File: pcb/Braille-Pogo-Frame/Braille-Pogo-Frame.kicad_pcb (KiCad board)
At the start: 2 copper layers, 74 x 40 mm, 24 parts, among them J101 Conn_01x06, J102 Conn_01x06, J103 Conn_01x06, J104 Conn_01x06, J105 Conn_01x06, J106 Conn_01x06, J107 Conn_01x06, J108 Conn_01x06

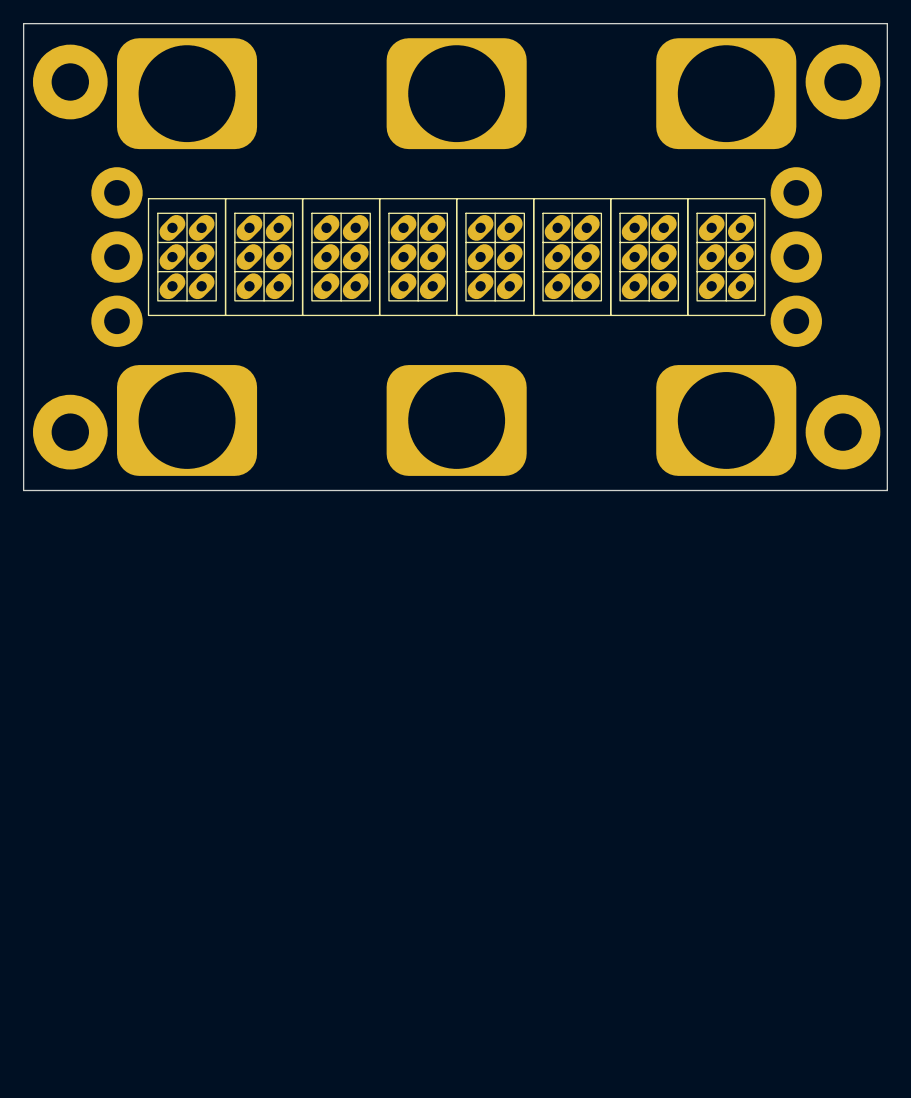
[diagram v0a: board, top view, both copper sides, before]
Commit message: Move PCB down
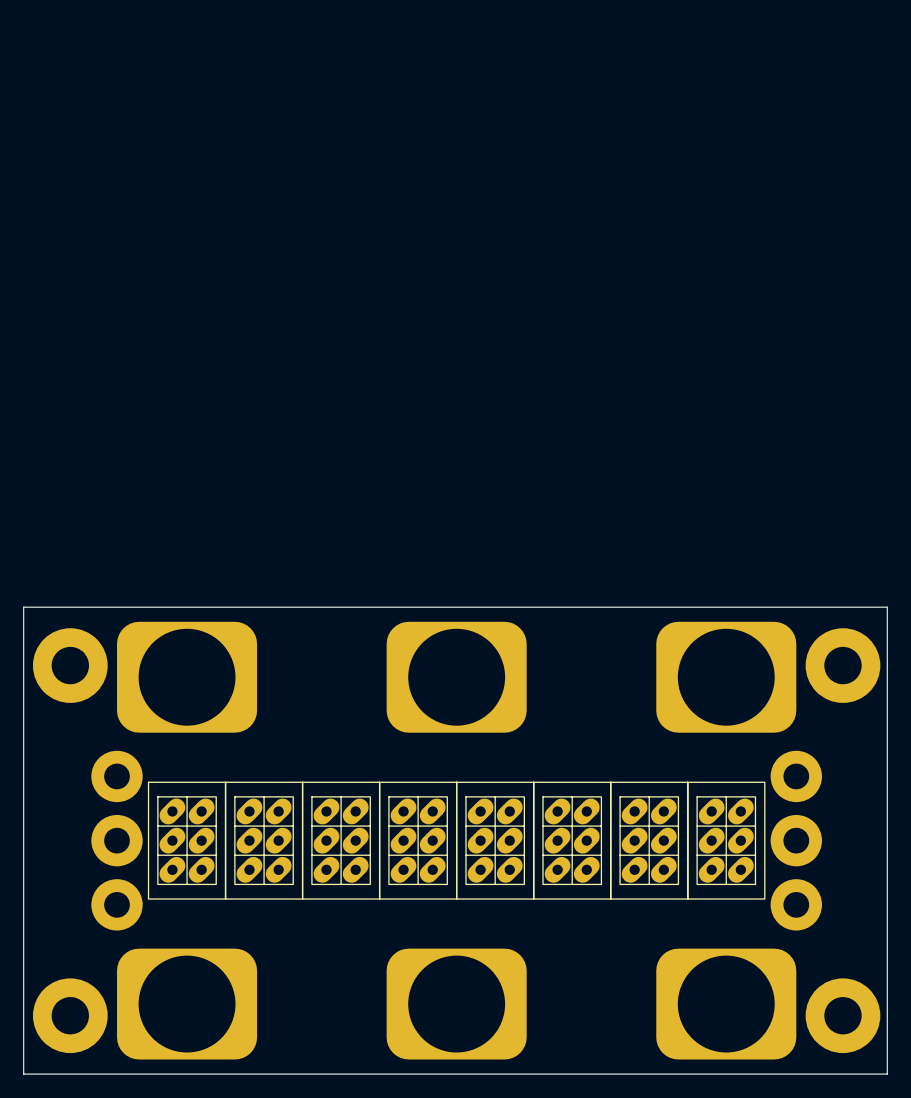
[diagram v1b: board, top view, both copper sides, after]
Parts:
- moved H101 50.0 mm to (123.1, 86.0)
- moved H102 50.0 mm to (123.1, 114.0)
- moved H103 50.0 mm to (146.2, 86.0)
- moved H104 50.0 mm to (100.0, 114.0)
- moved H105 50.0 mm to (100.0, 86.0)
- moved H106 50.0 mm to (146.2, 114.0)
- moved H107 50.0 mm to (94.0, 94.5)
- moved H108 50.0 mm to (94.0, 105.5)
- moved H109 50.0 mm to (152.2, 94.5)
- moved H110 50.0 mm to (152.2, 105.5)
- moved H111 50.0 mm to (94.0, 100.0)
- moved H112 50.0 mm to (152.2, 100.0)
- moved H113 50.0 mm to (90.0, 85.0)
- moved H114 50.0 mm to (156.2, 85.0)
- moved H115 50.0 mm to (156.2, 115.0)
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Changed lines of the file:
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@@
 	(footprint "00-lib-footprints:Braille_Cell_Pogos_Solder_2.5mmIntra_6.6x10mmInter"
 		(layer "F.Cu")
-		(at 100 50)
+		(at 100 100)
 		(property "Reference" "J101"
 			(at 0 5.1 0)
@@
 	(footprint "00-lib-footprints:Braille_Cell_Pogos_Solder_2.5mmIntra_6.6x10mmInter"
 		(layer "F.Cu")
-		(at 133 50)
+		(at 133 100)
 		(property "Reference" "J106"
 			(at 0 5.1 0)
@@
 	(footprint "00-lib-footprints:MountingHole_2.2mm_M2_Pad_NoSilk"
 		(layer "F.Cu")
-		(at 152.2 50)
+		(at 152.2 100)
 		(descr "Mounting Hole 2.2mm, M2")
 		(tags "mounting hole 2.2mm m2")
@@
 	(footprint "00-lib-footprints:MountingHole_8mm_Rect_NoSilk"
 		(layer "F.Cu")
-		(at 100 64)
+		(at 100 114)
 		(descr "Mounting Hole 8.4mm, M8")
 		(tags "mounting hole 8.4mm m8")
@@
 	(footprint "00-lib-footprints:MountingHole_2.2mm_M2_Pad_NoSilk"
 		(layer "F.Cu")
-		(at 152.2 55.5)
+		(at 152.2 105.5)
 		(descr "Mounting Hole 2.2mm, M2")
 		(tags "mounting hole 2.2mm m2")
@@
 	(footprint "00-lib-footprints:MountingHole_8mm_Rect_NoSilk"
 		(layer "F.Cu")
-		(at 146.2 64)
+		(at 146.2 114)
 		(descr "Mounting Hole 8.4mm, M8")
 		(tags "mounting hole 8.4mm m8")
@@
 	(footprint "00-lib-footprints:Braille_Cell_Pogos_Solder_2.5mmIntra_6.6x10mmInter"
 		(layer "F.Cu")
-		(at 139.6 50)
+		(at 139.6 100)
 		(property "Reference" "J107"
 			(at 0 5.1 0)
@@
 	(footprint "00-lib-footprints:MountingHole_2.2mm_M2_Pad_NoSilk"
 		(layer "F.Cu")
-		(at 94 44.5)
+		(at 94 94.5)
 		(descr "Mounting Hole 2.2mm, M2")
 		(tags "mounting hole 2.2mm m2")
@@
 	(footprint "00-lib-footprints:MountingHole_8mm_Rect_NoSilk"
 		(layer "F.Cu")
-		(at 146.2 36)
+		(at 146.2 86)
 		(descr "Mounting Hole 8.4mm, M8")
 		(tags "mounting hole 8.4mm m8")
@@
 	(footprint "00-lib-footprints:MountingHole_2.2mm_M2_Pad_NoSilk"
 		(layer "F.Cu")
-		(at 94 55.5)
+		(at 94 105.5)
 		(descr "Mounting Hole 2.2mm, M2")
 		(tags "mounting hole 2.2mm m2")
@@
 	(footprint "00-lib-footprints:Braille_Cell_Pogos_Solder_2.5mmIntra_6.6x10mmInter"
 		(layer "F.Cu")
-		(at 106.6 50)
+		(at 106.6 100)
 		(property "Reference" "J103"
 			(at 0 5.1 0)
@@
 	(footprint "00-lib-footprints:MountingHole_8mm_Rect_NoSilk"
 		(layer "F.Cu")
-		(at 123.1 36)
+		(at 123.1 86)
 		(descr "Mounting Hole 8.4mm, M8")
 		(tags "mounting hole 8.4mm m8")
@@
 	(footprint "00-lib-footprints:Braille_Cell_Pogos_Solder_2.5mmIntra_6.6x10mmInter"
 		(layer "F.Cu")
-		(at 146.2 50)
+		(at 146.2 100)
 		(property "Reference" "J108"
 			(at 0 5.1 0)
@@
 	(footprint "00-lib-footprints:MountingHole_2.2mm_M2_Pad_NoSilk"
 		(layer "F.Cu")
-		(at 94 50)
+		(at 94 100)
 		(descr "Mounting Hole 2.2mm, M2")
 		(tags "mounting hole 2.2mm m2")
@@
 	(footprint "00-lib-footprints:Braille_Cell_Pogos_Solder_2.5mmIntra_6.6x10mmInter"
 		(layer "F.Cu")
-		(at 113.2 50)
+		(at 113.2 100)
 		(property "Reference" "J102"
 			(at 0 5.1 0)
@@
 	(footprint "00-lib-footprints:MountingHole_2.2mm_M2_Pad_NoSilk"
 		(layer "F.Cu")
-		(at 152.2 44.5)
+		(at 152.2 94.5)
 		(descr "Mounting Hole 2.2mm, M2")
 		(tags "mounting hole 2.2mm m2")
@@
 	(footprint "00-lib-footprints:MountingHole_3.2mm_M3_Pad_NoSilk"
 		(layer "F.Cu")
-		(at 156.2 65)
+		(at 156.2 115)
 		(descr "Mounting Hole 3.2mm, M3")
 		(tags "mounting hole 3.2mm m3")
@@
 	(footprint "00-lib-footprints:MountingHole_8mm_Rect_NoSilk"
 		(layer "F.Cu")
-		(at 123.1 64)
+		(at 123.1 114)
 		(descr "Mounting Hole 8.4mm, M8")
 		(tags "mounting hole 8.4mm m8")
@@
 	(footprint "00-lib-footprints:MountingHole_3.2mm_M3_Pad_NoSilk"
 		(layer "F.Cu")
-		(at 90 35)
+		(at 90 85)
 		(descr "Mounting Hole 3.2mm, M3")
 		(tags "mounting hole 3.2mm m3")
@@
 	(footprint "00-lib-footprints:MountingHole_3.2mm_M3_Pad_NoSilk"
 		(layer "F.Cu")
-		(at 156.2 35)
+		(at 156.2 85)
 		(descr "Mounting Hole 3.2mm, M3")
 		(tags "mounting hole 3.2mm m3")
@@
 	(footprint "00-lib-footprints:MountingHole_3.2mm_M3_Pad_NoSilk"
 		(layer "F.Cu")
-		(at 90 65)
+		(at 90 115)
 		(descr "Mounting Hole 3.2mm, M3")
 		(tags "mounting hole 3.2mm m3")
@@
 	(footprint "00-lib-footprints:MountingHole_8mm_Rect_NoSilk"
 		(layer "F.Cu")
-		(at 100 36)
+		(at 100 86)
 		(descr "Mounting Hole 8.4mm, M8")
 		(tags "mounting hole 8.4mm m8")
@@
 	(footprint "00-lib-footprints:Braille_Cell_Pogos_Solder_2.5mmIntra_6.6x10mmInter"
 		(layer "F.Cu")
-		(at 119.8 50)
+		(at 119.8 100)
 		(property "Reference" "J104"
 			(at 0 5.1 0)
@@
 	(footprint "00-lib-footprints:Braille_Cell_Pogos_Solder_2.5mmIntra_6.6x10mmInter"
 		(layer "F.Cu")
-		(at 126.4 50)
+		(at 126.4 100)
 		(property "Reference" "J105"
 			(at 0 5.1 0)
@@
 	)
 	(gr_rect
-		(start 121.75 41)
-		(end 148 44.5)
+		(start 121.75 91)
+		(end 148 94.5)
 		(stroke
 			(width 0.1)
@@
 	)
 	(gr_rect
-		(start 105.5 40)
-		(end 117 44.5)
+		(start 105.5 90)
+		(end 117 94.5)
 		(stroke
 			(width 0.1)
@@
 	)
 	(gr_rect
-		(start 86 30)
-		(end 160 70)
+		(start 86 80)
+		(end 160 120)
 		(stroke
 			(width 0.05)
@@
 	)
 	(gr_text "Braille Display (Pogo + Solenoid)\n2024-10-10"
-		(at 148 44.25 0)
+		(at 148 94.25 0)
 		(layer "B.SilkS")
 		(effects
@@
 	)
 	(gr_text "6.6mm Inter-Cell\n2.5mm Intra-Cell\nM2, M3, and 8mm"
-		(at 116.75 44 0)
+		(at 116.75 94 0)
 		(layer "B.SilkS")
 		(effects

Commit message: Refactor Braille Cells, add Stepper footprint
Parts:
- renumbered H101 to H1, H110 to H10, H111 to H11, H112 to H12, H113 to H13, H114 to H14, H115 to H15, H116 to H16, H102 to H2, H103 to H3, H104 to H4, H105 to H5, H106 to H6, H107 to H7, H108 to H8, H109 to H9, J101 to J1, J102 to J2, J103 to J3, J104 to J4, J105 to J5, J106 to J6, J107 to J7, J108 to J8

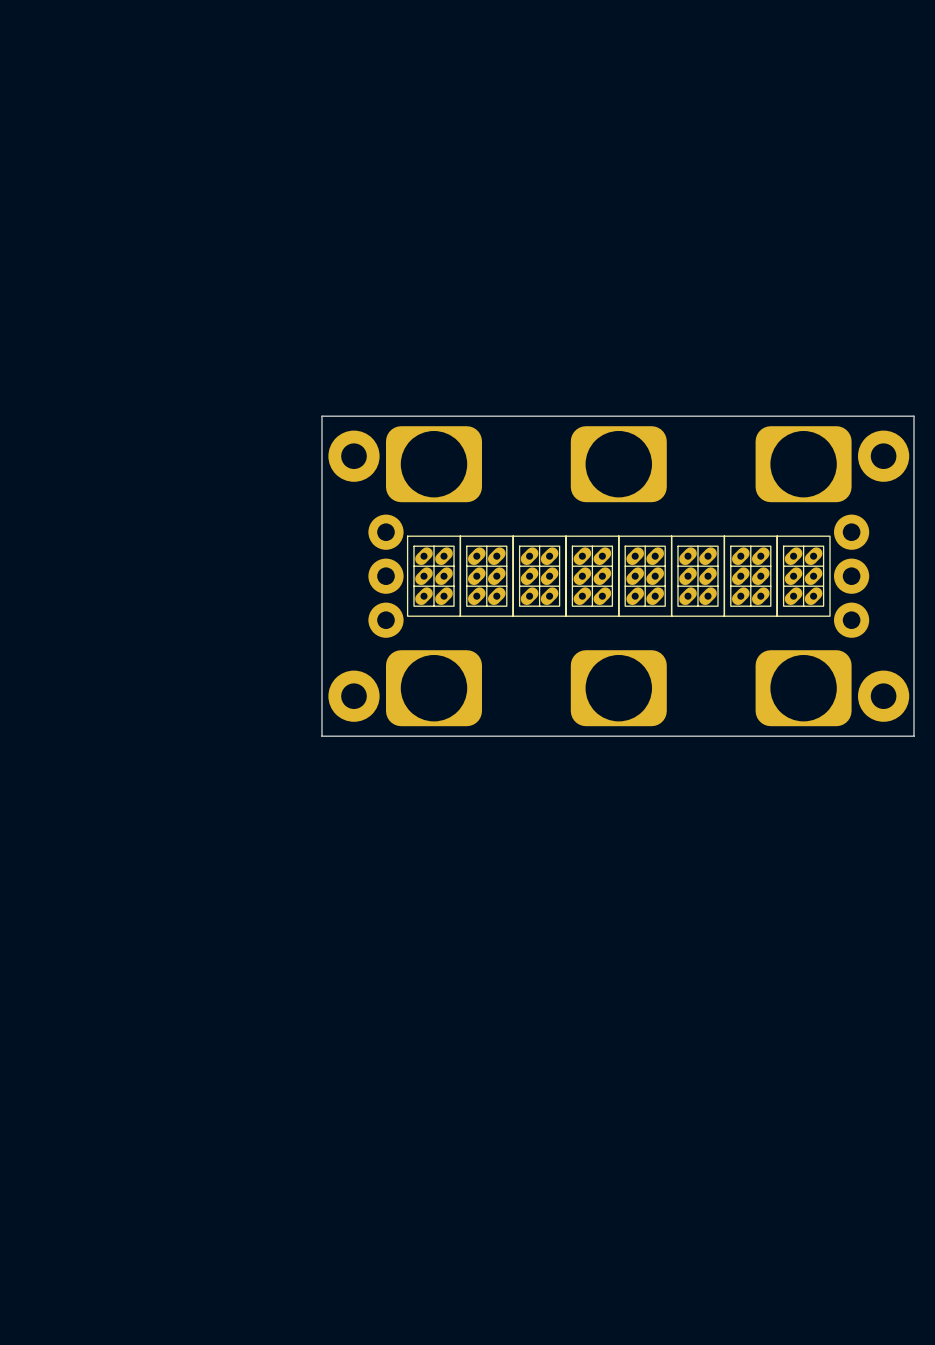
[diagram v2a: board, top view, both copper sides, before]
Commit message: PCB: Place motor drivers and horiz. rail mounts
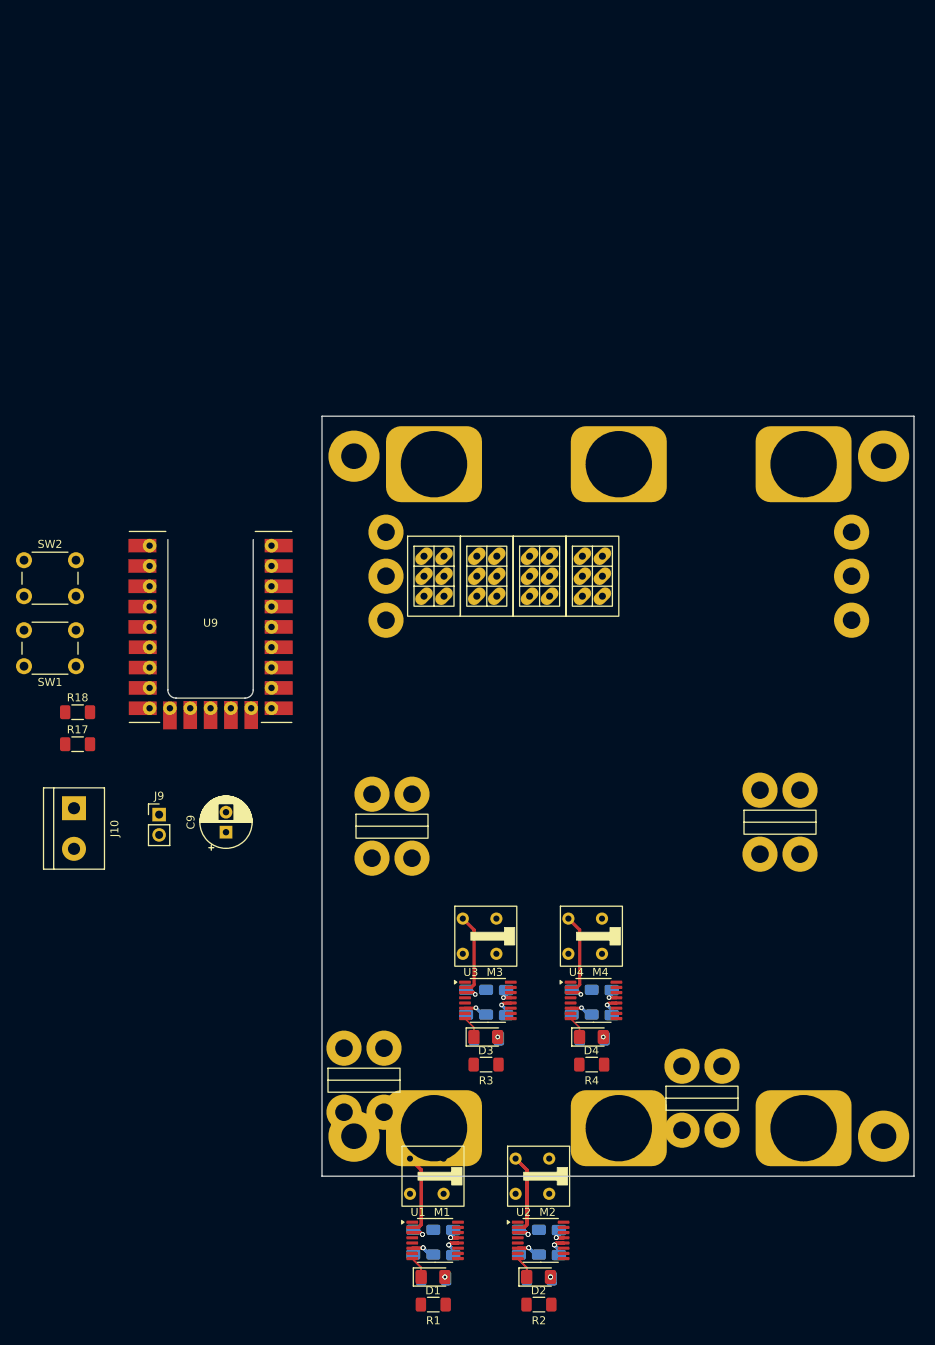
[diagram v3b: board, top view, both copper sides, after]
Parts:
- removed J5, J6, J7, J8: Conn_01x06, 00-lib-footprints:Braille_Cell_Pogos_Solder_2.5mmIntra_6.6x10mmInter
- added C1: 100n, Capacitor_SMD:C_1206_3216Metric_Pad1.33x1.80mm_HandSolder, B.Cu at (102.4, 183.3)
- added C2: 100n, Capacitor_SMD:C_1206_3216Metric_Pad1.33x1.80mm_HandSolder, B.Cu at (115.6, 183.3)
- added C3: 100n, Capacitor_SMD:C_1206_3216Metric_Pad1.33x1.80mm_HandSolder, B.Cu at (109.0, 153.3)
- added C4: 100n, Capacitor_SMD:C_1206_3216Metric_Pad1.33x1.80mm_HandSolder, B.Cu at (122.2, 153.3)
- added C9: 10u, Capacitor_THT:CP_Radial_D6.3mm_P2.50mm, F.Cu at (74.0, 132.0)
- added D1: LED, LED_SMD:LED_1206_3216Metric_Pad1.42x1.75mm_HandSolder, F.Cu at (99.9, 187.6)
- added D2: LED, LED_SMD:LED_1206_3216Metric_Pad1.42x1.75mm_HandSolder, F.Cu at (113.1, 187.6)
- added D3: LED, LED_SMD:LED_1206_3216Metric_Pad1.42x1.75mm_HandSolder, F.Cu at (106.5, 157.6)
- added D4: LED, LED_SMD:LED_1206_3216Metric_Pad1.42x1.75mm_HandSolder, F.Cu at (119.7, 157.6)
- added H17: MountingHole_Pad, 00-lib-footprints:HorizMounting_4x_M2_and_M3_Middle, F.Cu at (94.8, 131.2)
- added H18: MountingHole_Pad, 00-lib-footprints:HorizMounting_4x_M2_and_M3_Middle, F.Cu at (91.2, 163.0)
- added H19: MountingHole_Pad, 00-lib-footprints:HorizMounting_4x_M2_and_M3_Middle, F.Cu at (143.2, 130.8)
- added H20: MountingHole_Pad, 00-lib-footprints:HorizMounting_4x_M2_and_M3_Middle, F.Cu at (133.5, 165.2)
- added J10: Screw_Terminal_01x02, TerminalBlock:TerminalBlock_bornier-2_P5.08mm, F.Cu at (55.0, 129.0)
- added J9: Conn_01x02, Connector_PinHeader_2.54mm:PinHeader_1x02_P2.54mm_Vertical, F.Cu at (65.6, 129.8)
- added M1: Stepper_Motor_bipolar, 00-lib-footprints:MicroStepper_8mm-2mmGear, F.Cu at (100.0, 175.0)
- added M2: Stepper_Motor_bipolar, 00-lib-footprints:MicroStepper_8mm-2mmGear, F.Cu at (113.2, 175.0)
- added M3: Stepper_Motor_bipolar, 00-lib-footprints:MicroStepper_8mm-2mmGear, F.Cu at (106.6, 145.0)
- added M4: Stepper_Motor_bipolar, 00-lib-footprints:MicroStepper_8mm-2mmGear, F.Cu at (119.8, 145.0)
- added R1: 5k1, Resistor_SMD:R_1206_3216Metric_Pad1.30x1.75mm_HandSolder, F.Cu at (99.9, 191.1)
- added R10: 2k1, Resistor_SMD:R_1206_3216Metric_Pad1.30x1.75mm_HandSolder, B.Cu at (113.2, 187.8)
- added R11: 2k1, Resistor_SMD:R_1206_3216Metric_Pad1.30x1.75mm_HandSolder, B.Cu at (106.6, 157.8)
- added R12: 2k1, Resistor_SMD:R_1206_3216Metric_Pad1.30x1.75mm_HandSolder, B.Cu at (119.8, 157.8)
- added R17: 5k1, Resistor_SMD:R_1206_3216Metric_Pad1.30x1.75mm_HandSolder, F.Cu at (55.5, 121.0)
- added R18: 5k1, Resistor_SMD:R_1206_3216Metric_Pad1.30x1.75mm_HandSolder, F.Cu at (55.5, 117.0)
- added R19: 330m, Resistor_SMD:R_1206_3216Metric_Pad1.30x1.75mm_HandSolder, B.Cu at (99.9, 183.2)
- added R2: 5k1, Resistor_SMD:R_1206_3216Metric_Pad1.30x1.75mm_HandSolder, F.Cu at (113.1, 191.1)
- added R20: 330m, Resistor_SMD:R_1206_3216Metric_Pad1.30x1.75mm_HandSolder, B.Cu at (113.1, 183.2)
- added R21: 330m, Resistor_SMD:R_1206_3216Metric_Pad1.30x1.75mm_HandSolder, B.Cu at (106.5, 153.2)
- added R22: 330m, Resistor_SMD:R_1206_3216Metric_Pad1.30x1.75mm_HandSolder, B.Cu at (119.7, 153.2)
- added R27: 330m, Resistor_SMD:R_1206_3216Metric_Pad1.30x1.75mm_HandSolder, B.Cu at (97.4, 183.2)
- added R28: 330m, Resistor_SMD:R_1206_3216Metric_Pad1.30x1.75mm_HandSolder, B.Cu at (110.6, 183.2)
- added R29: 330m, Resistor_SMD:R_1206_3216Metric_Pad1.30x1.75mm_HandSolder, B.Cu at (104.0, 153.2)
- added R3: 5k1, Resistor_SMD:R_1206_3216Metric_Pad1.30x1.75mm_HandSolder, F.Cu at (106.5, 161.1)
- added R30: 330m, Resistor_SMD:R_1206_3216Metric_Pad1.30x1.75mm_HandSolder, B.Cu at (117.2, 153.2)
- added R4: 5k1, Resistor_SMD:R_1206_3216Metric_Pad1.30x1.75mm_HandSolder, F.Cu at (119.7, 161.1)
- added R9: 2k1, Resistor_SMD:R_1206_3216Metric_Pad1.30x1.75mm_HandSolder, B.Cu at (100.0, 187.8)
- added SW1: SW_Push, Button_Switch_THT:SW_PUSH_6mm, F.Cu at (55.2, 111.2)
- added SW2: SW_Push, Button_Switch_THT:SW_PUSH_6mm, F.Cu at (48.8, 98.0)
- added U1: DRV8847SPWR, Package_SO:TSSOP-16_4.4x5mm_P0.65mm, F.Cu at (100.1, 183.0)
- added U2: DRV8847SPWR, Package_SO:TSSOP-16_4.4x5mm_P0.65mm, F.Cu at (113.3, 183.0)
- added U3: DRV8847SPWR, Package_SO:TSSOP-16_4.4x5mm_P0.65mm, F.Cu at (106.7, 153.0)
- added U4: DRV8847SPWR, Package_SO:TSSOP-16_4.4x5mm_P0.65mm, F.Cu at (119.9, 153.0)
- added U9: RP2040-Zero, 00-lib-footprints:RP2040 Zero, F.Cu at (61.9, 119.2)
- moved H15 55.0 mm to (156.2, 170.0)
- moved H16 55.0 mm to (90.0, 170.0)
- moved H2 55.0 mm to (123.1, 169.0)
- moved H4 55.0 mm to (100.0, 169.0)
- moved H6 55.0 mm to (146.2, 169.0)
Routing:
- net Net-(U2-OUT1): track 0.00 -> 20.2 mm
- net Net-(U1-OUT1): track 0.00 -> 20.2 mm
- net Vdrive: track 0.00 -> 16.6 mm, vias 0 -> 6
- net GND: track 0.00 -> 12.1 mm, vias 0 -> 6
- net Net-(U3-OUT1): track 0.00 -> 10.1 mm
- net Net-(U4-OUT1): track 0.00 -> 10.1 mm
- net Net-(U2-ISEN34): track 0.00 -> 6.02 mm, vias 0 -> 2
- net Net-(U1-ISEN34): track 0.00 -> 6.02 mm, vias 0 -> 2
- net /Braille_Cell1/~{FAULT}: track 0.00 -> 5.52 mm
- net /Braille_Cell/~{FAULT}: track 0.00 -> 5.52 mm
- net Net-(U2-ISEN12): track 0.00 -> 5.52 mm, vias 0 -> 2
- net Net-(U1-ISEN12): track 0.00 -> 5.52 mm, vias 0 -> 2
- net Net-(U4-ISEN34): track 0.00 -> 3.01 mm, vias 0 -> 1
- net Net-(U3-ISEN34): track 0.00 -> 3.01 mm, vias 0 -> 1
- net /Braille_Cell3/~{FAULT}: track 0.00 -> 2.76 mm
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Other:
- board size 74 x 40 mm -> 74 x 95 mm
